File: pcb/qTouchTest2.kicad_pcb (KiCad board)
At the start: 2 copper layers, 68.5 x 47 mm, 40 parts, among them CON1 AVR-ISP-6, J1 USB-MINI-B, K1 CONN_3, P1 CONN_1, P2 CONN_1, P3 CONN_1, P6 CONN_1, P7 CONN_1, P8 CONN_1, P9 CONN_1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

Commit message: adding ferrite bead and crystal info
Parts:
- L1: value INDUCTOR -> FERRITE_BEAD
- X1: value CRYSTAL -> CRYSTAL_8MHz

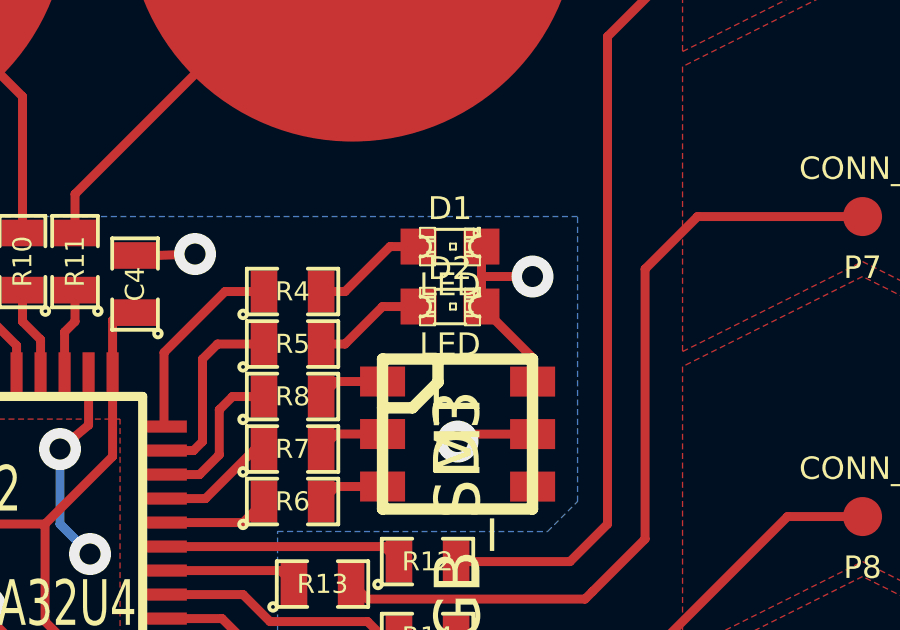
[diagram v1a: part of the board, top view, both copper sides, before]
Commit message: adding colour info to LEDs
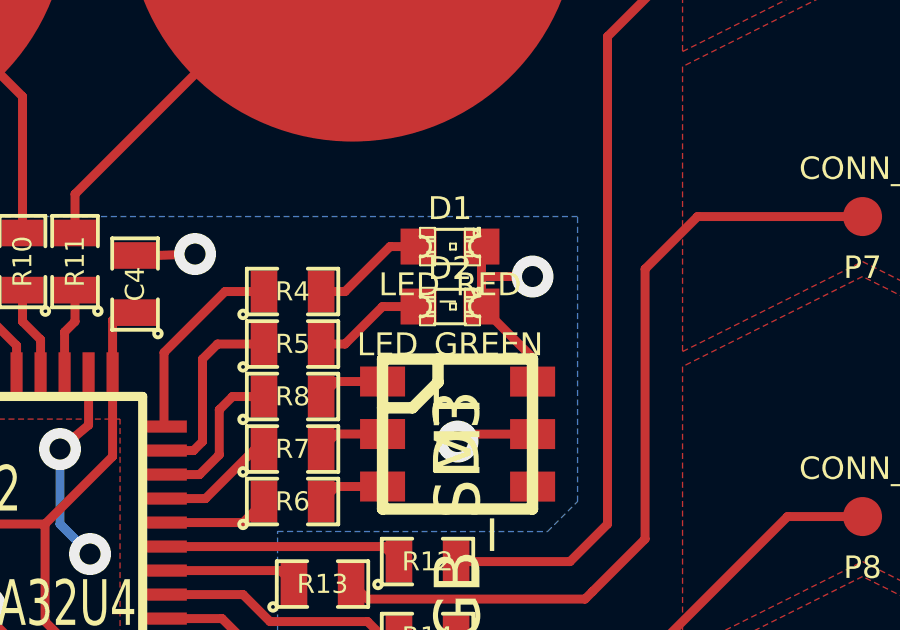
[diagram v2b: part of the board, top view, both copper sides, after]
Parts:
- D1: value LED -> LED_RED
- D2: value LED -> LED_GREEN

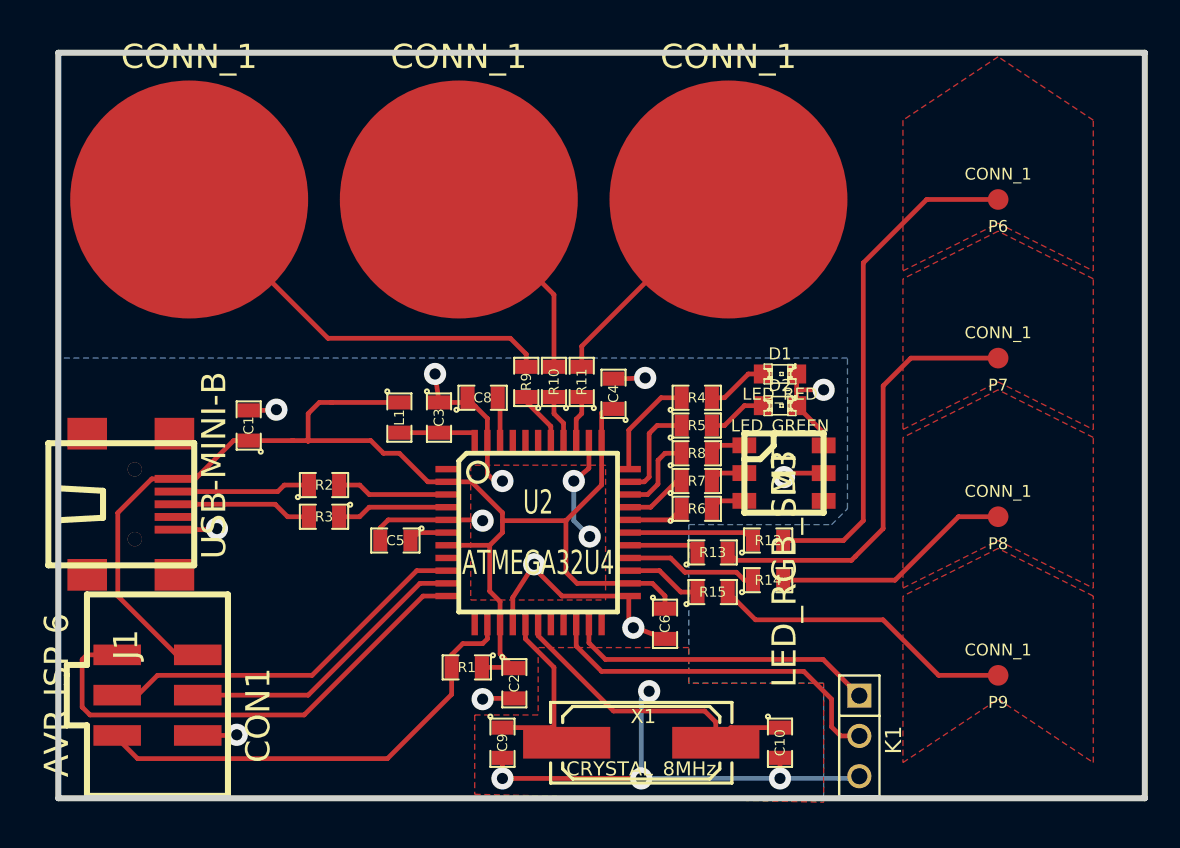
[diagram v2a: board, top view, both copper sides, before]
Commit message: adding rev2 text, one trace thickness modified
track to P6 thickness doubled as sensitivity was
below others
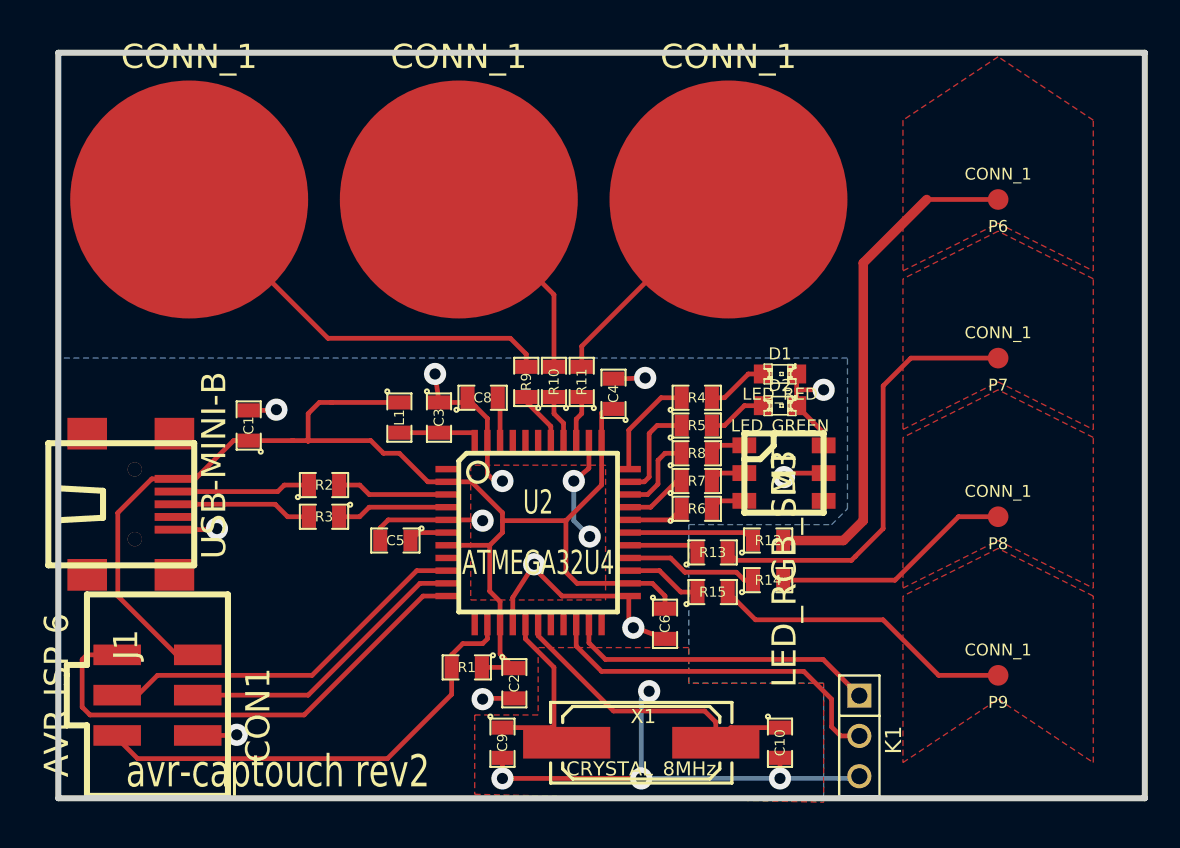
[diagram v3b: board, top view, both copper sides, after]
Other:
- board text added: "avr-captouch rev2"
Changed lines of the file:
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@@
     (area 43.48226 39.83228 113.441481 89.27592)
     (thickness 1.6002)
-    (drawings 4)
+    (drawings 5)
     (tracks 268)
     (zones 0)
@@
   )
   (page A4)
+  (title_block
+    (rev 2)
+  )
   (layers
     (15 Front signal)
@@
   )
   (setup
-    (last_trace_width 0.29972)
+    (last_trace_width 0.6)
+    (user_trace_width 0.6)
     (trace_clearance 0.254)
     (zone_clearance 0.39878)
@@
     (visible_elements 7FFFFFFF)
     (pcbplotparams
-      (layerselection 268468225)
+      (layerselection 272138241)
       (usegerberextensions true)
       (excludeedgelayer true)
@@
       (psa4output false)
       (plotreference true)
-      (plotvalue true)
+      (plotvalue false)
       (plotothertext true)
       (plotinvisibletext false)
       (padsonsilk false)
-      (subtractmaskfromsilk false)
+      (subtractmaskfromsilk true)
       (outputformat 1)
       (mirror false)
-      (drillshape 1)
+      (drillshape 0)
       (scaleselection 1)
       (outputdirectory gerbers/))
@@
       (rotate (xyz 0 0 0))
     )
+  )
+  (gr_text "avr-captouch rev2\n" (at 58.59 86.06) (layer F.SilkS)
+    (effects (font (size 2.032 1.524) (thickness 0.3048)))
   )
   (gr_line (start 44.74972 87.74938) (end 113.25098 87.74938) (angle 90) (layer Edge.Cuts) (width 0.381))
@@
   (segment (start 82.09788 69.40042) (end 83.74888 67.74942) (width 0.29972) (layer Front) (net 10))
   (segment (start 83.74888 67.74942) (end 84.0486 67.74942) (width 0.29972) (layer Front) (net 10))
-  (segment (start 95.49892 70.25132) (end 95.49892 54.0004) (width 0.29972) (layer Front) (net 11))
-  (segment (start 95.49892 54.0004) (end 99.49942 49.9999) (width 0.29972) (layer Front) (net 11))
-  (segment (start 94.24924 71.501) (end 95.49892 70.25132) (width 0.29972) (layer Front) (net 11))
+  (segment (start 95.49892 70.25132) (end 95.49892 54.0004) (width 0.6) (layer Front) (net 11))
+  (segment (start 95.49892 54.0004) (end 99.49942 49.9999) (width 0.6) (layer Front) (net 11))
+  (segment (start 94.24924 71.501) (end 95.49892 70.25132) (width 0.6) (layer Front) (net 11))
   (segment (start 99.49942 49.9999) (end 104.0003 49.9999) (width 0.29972) (layer Front) (net 11))
-  (segment (start 90.45194 71.501) (end 94.24924 71.501) (width 0.29972) (layer Front) (net 11))
+  (segment (start 90.45194 71.501) (end 94.24924 71.501) (width 0.6) (layer Front) (net 11))
   (segment (start 87.50046 72.75068) (end 94.74962 72.75068) (width 0.29972) (layer Front) (net 12))
   (segment (start 98.5012 59.99988) (end 96.75114 61.74994) (width 0.29972) (layer Front) (net 12))
